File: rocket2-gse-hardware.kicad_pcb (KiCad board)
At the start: 4 copper layers, 118 x 135.2 mm, 194 parts, among them J1 USB_C Connector, Q1 n-MOSFET, Q10 n-MOSFET, Q2 n-MOSFET, Q3 n-MOSFET, Q4 n-MOSFET, Q5 n-MOSFET, Q6 n-MOSFET, Q7 n-MOSFET, Q8 n-MOSFET, Q9 n-MOSFET, Y1 16MHz

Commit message: finished pcb design of gse 1.0
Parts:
- removed PWR: Conn_01x02_Pin, TerminalBlock:TerminalBlock_bornier-2_P5.08mm
- removed S9: Solenoid, TerminalBlock:TerminalBlock_bornier-3_P5.08mm
- added C41: 100nF, Capacitor_SMD:C_0402_1005Metric, F.Cu at (200.5, 160.5)
- added C42: 100nF, Capacitor_SMD:C_0402_1005Metric, F.Cu at (185.5, 160.5)
- added D21: 3.3V, Diode_SMD:D_SOD-123, F.Cu at (99.0, 81.9)
- added D22: 1.0A, Diode_SMD:D_SMA, F.Cu at (91.5, 93.0)
- added D31: 3.3V, Diode_SMD:D_SOD-123, F.Cu at (99.1, 146.9)
- added D32: 5.1V, Diode_SMD:D_MiniMELF, F.Cu at (170.0, 143.5)
- added D33: 5.1V, Diode_SMD:D_MiniMELF, F.Cu at (131.0, 143.5)
- added D34: 5.1V, Diode_SMD:D_MiniMELF, F.Cu at (118.0, 143.5)
- added D35: 5.1V, Diode_SMD:D_MiniMELF, F.Cu at (144.0, 143.5)
- added D36: 5.1V, Diode_SMD:D_MiniMELF, F.Cu at (157.0, 143.5)
- added F1: Fuse Holder, Fuse:Fuseholder_Blade_Mini_Keystone_3568, F.Cu at (116.0, 28.3)
- added J2: ALARM, TerminalBlock:TerminalBlock_bornier-2_P5.08mm, F.Cu at (222.5, 162.0)
- added J3: USB_C Connector, Connector_USB:USB_C_Receptacle_GCT_USB4105-xx-A_16P_TopMnt_Horizontal, F.Cu at (171.0, 24.3)
- added J4: PWR, Connector_BarrelJack:BarrelJack_Horizontal, F.Cu at (142.0, 34.5)
- added J5: PWR, Connector_BarrelJack:BarrelJack_Horizontal, F.Cu at (157.0, 34.5)
- added J6: E-MATCH, TerminalBlock:TerminalBlock_bornier-2_P5.08mm, F.Cu at (197.0, 162.0)
- added J7: E-MATCH, TerminalBlock:TerminalBlock_bornier-2_P5.08mm, F.Cu at (182.0, 162.0)
- added PT4: Pressure Transducer 1, TerminalBlock:TerminalBlock_bornier-3_P5.08mm, F.Cu at (167.0, 163.1)
- added Q11: 30V 4A, Package_TO_SOT_SMD:SOT-23-3, F.Cu at (198.7, 153.1)
- added Q12: 30V 4A, Package_TO_SOT_SMD:SOT-23-3, F.Cu at (192.0, 153.2)
- added Q13: 30V 4A, Package_TO_SOT_SMD:SOT-23-3, F.Cu at (183.7, 153.1)
- added Q14: 30V 4A, Package_TO_SOT_SMD:SOT-23-3, F.Cu at (177.0, 153.2)
- added R54: 1K, Resistor_SMD:R_0402_1005Metric, F.Cu at (101.3, 143.8)
- added R55: 1K, Resistor_SMD:R_0402_1005Metric, F.Cu at (166.8, 148.0)
- added R56: 5K, Resistor_SMD:R_0402_1005Metric, F.Cu at (166.8, 140.0)
- added R57: 10K, Resistor_SMD:R_0402_1005Metric, F.Cu at (164.2, 140.0)
- added R58: 1K, Resistor_SMD:R_0402_1005Metric, F.Cu at (127.8, 148.0)
- added R59: 5K, Resistor_SMD:R_0402_1005Metric, F.Cu at (127.8, 140.0)
- added R60: 10K, Resistor_SMD:R_0402_1005Metric, F.Cu at (125.2, 140.0)
- added R61: 1K, Resistor_SMD:R_0402_1005Metric, F.Cu at (114.8, 148.0)
- added R62: 5K, Resistor_SMD:R_0402_1005Metric, F.Cu at (114.8, 140.0)
- added R63: 10K, Resistor_SMD:R_0402_1005Metric, F.Cu at (112.2, 140.0)
- added R64: 1K, Resistor_SMD:R_0402_1005Metric, F.Cu at (140.8, 148.0)
- added R65: 5K, Resistor_SMD:R_0402_1005Metric, F.Cu at (140.8, 140.0)
- added R66: 10K, Resistor_SMD:R_0402_1005Metric, F.Cu at (138.2, 140.0)
- added R67: 1K, Resistor_SMD:R_0402_1005Metric, F.Cu at (153.8, 148.0)
- added R68: 5K, Resistor_SMD:R_0402_1005Metric, F.Cu at (153.8, 140.0)
- added R69: 10K, Resistor_SMD:R_0402_1005Metric, F.Cu at (151.2, 140.0)
- added R70: 10K, Resistor_SMD:R_0402_1005Metric, F.Cu at (196.2, 153.9)
- added R71: 10K, Resistor_SMD:R_0402_1005Metric, F.Cu at (198.7, 150.0)
- added R72: 33K, Resistor_SMD:R_0402_1005Metric, F.Cu at (192.5, 156.1)
- added R73: 100, Resistor_SMD:R_0402_1005Metric, F.Cu at (192.5, 150.2)
- added R74: 10K, Resistor_SMD:R_0402_1005Metric, F.Cu at (190.0, 150.2)
- added R75: 10K, Resistor_SMD:R_0402_1005Metric, F.Cu at (181.2, 153.9)
- added R76: 10K, Resistor_SMD:R_0402_1005Metric, F.Cu at (183.7, 150.0)
- added R77: 33K, Resistor_SMD:R_0402_1005Metric, F.Cu at (177.5, 156.1)
- added R78: 100, Resistor_SMD:R_0402_1005Metric, F.Cu at (177.5, 150.2)
- added R79: 10K, Resistor_SMD:R_0402_1005Metric, F.Cu at (175.0, 150.2)
- added TP4: TestPoint, TestPoint:TestPoint_Pad_D2.0mm, F.Cu at (191.4, 88.8)
- added TP5: TestPoint, TestPoint:TestPoint_Pad_D2.0mm, F.Cu at (191.4, 93.8)
- added TP6: TestPoint, TestPoint:TestPoint_Pad_D2.0mm, F.Cu at (191.4, 98.8)
- C10: value 100nF -> 10uF
- C11, C13, C14, C9: value 100nF -> 1uF
- C25, C27: value 10nF -> 100nF
- C36: value 10uF -> 100nF
- C37: value 0.33uF -> 10nF
- C39, C8: value 1uF -> 10nF
- C40: value 1uF -> 100nF
- C6: value 4.7uF -> 100nF
- C7: value 10nF -> 4.7uF
- D1, D3, D5: value 1.0A -> LED; footprint Diode_SMD:D_SMA -> LED_SMD:LED_0603_1608Metric
- D10, D12, D6, D8: value 1.8V -> 3A 100V; footprint Diode_SMD:D_SOD-123 -> Diode_SMD:D_SMA
- D11, D13, D7, D9: value 1.0A -> 3A 100V
- D14, D16, D18, D20: value 1.8V -> 1.0A; footprint Diode_SMD:D_SOD-123 -> Diode_SMD:D_SMA
- D15, D17, D19: value 1.0A -> 3.3V; footprint Diode_SMD:D_SMA -> Diode_SMD:D_SOD-123
- D2, D4: value 1.8V -> LED; footprint Diode_SMD:D_SOD-123 -> LED_SMD:LED_0603_1608Metric
- D23, D25: value 5V -> 3.3V; footprint Diode_SMD:D_MiniMELF -> Diode_SMD:D_SOD-123
- D24, D26: value 5V -> 1.0A; footprint Diode_SMD:D_MiniMELF -> Diode_SMD:D_SMA
- D27, D29: value LED -> 3.3V; footprint LED_SMD:LED_0603_1608Metric -> Diode_SMD:D_SOD-123
- D28, D30: value LED -> 1.0A; footprint LED_SMD:LED_0603_1608Metric -> Diode_SMD:D_SMA
- J1: value USB_C Connector -> ARMING_PLUG; footprint Connector_USB:USB_C_Receptacle_GCT_USB4105-xx-A_16P_TopMnt_Horizontal -> TerminalBlock:TerminalBlock_bornier-2_P5.08mm
- Q1, Q10, Q2, Q3, Q4, Q5, Q6, Q7, Q8, Q9: value n-MOSFET -> 30V 4A
- R10: value 1K -> 3.3K
- R12, R24: value 1 -> 100; footprint Resistor_SMD:R_1206_3216Metric -> Resistor_SMD:R_0402_1005Metric
- R13, R7: value 1K -> 100K
- R14: value 10K -> 15K
- R15: value 1 -> 5K1; footprint Resistor_SMD:R_1206_3216Metric -> Resistor_SMD:R_0402_1005Metric
- R16: value 1K -> 5K1
- R17, R2: value 10K -> 100K
- R18, R9: value 1 -> 15K; footprint Resistor_SMD:R_1206_3216Metric -> Resistor_SMD:R_0402_1005Metric
- R19, R31, R35: value 1K -> 10K
- R20: value 10K -> 100
- R25, R41: value 1K -> 1; footprint Resistor_SMD:R_0402_1005Metric -> Resistor_SMD:R_1206_3216Metric
- R26, R5: value 10K -> 1K
- R27: value 1 -> 10K; footprint Resistor_SMD:R_1206_3216Metric -> Resistor_SMD:R_0402_1005Metric
- R28, R32: value 1K -> 100
- R29, R45: value 10K -> 1; footprint Resistor_SMD:R_0402_1005Metric -> Resistor_SMD:R_1206_3216Metric
- R3: value 1 -> 100K; footprint Resistor_SMD:R_1206_3216Metric -> Resistor_SMD:R_0402_1005Metric
- R30: value 1 -> 1K; footprint Resistor_SMD:R_1206_3216Metric -> Resistor_SMD:R_0402_1005Metric
- R33, R37: value 4.7K -> 1; footprint Resistor_SMD:R_0402_1005Metric -> Resistor_SMD:R_1206_3216Metric
- R34, R42: value 4.7K -> 1K
- R36, R40: value 4.7K -> 100
- R39, R43: value 4.7K -> 10K
- R4: value 1K -> 470
- R44: value 70K -> 100
- R46: value 100K -> 1K
- R47: value 100K -> 10K
- R48: value 470 -> 100
- R49: value 220 -> 1; footprint Resistor_SMD:R_0402_1005Metric -> Resistor_SMD:R_1206_3216Metric
- R50: value 470 -> 1K
- R51: value 2K -> 10K
- R52: value 5K1 -> 100
- R53: value 5K1 -> 1; footprint Resistor_SMD:R_0402_1005Metric -> Resistor_SMD:R_1206_3216Metric
- R6: value 1 -> 3.3K; footprint Resistor_SMD:R_1206_3216Metric -> Resistor_SMD:R_0402_1005Metric
- R8: value 10K -> 3.3K
- U16, U17, U18: footprint Package_SO:SOIC-8_3.9x4.9mm_P1.27mm -> Package_TO_SOT_SMD:SOT-23-6
- U2: footprint Package_TO_SOT_SMD:SOT-23-6 -> UCIRP-KiCAD-Lib:GC-XPORT
- U22: footprint UCIRP-KiCAD-Lib:GC-XPORT -> Package_SO:SOIC-8_3.9x4.9mm_P1.27mm
- U23: footprint Package_TO_SOT_SMD:SOT-89-3 -> Package_SO:SOIC-8_3.9x4.9mm_P1.27mm
- U24: footprint Package_TO_SOT_SMD:SOT-23-3 -> Package_SO:SOIC-8_3.9x4.9mm_P1.27mm
- U3: footprint Package_TO_SOT_SMD:SOT-23-6 -> Package_TO_SOT_SMD:SOT-89-3
- U4: footprint Package_TO_SOT_SMD:SOT-23-6 -> Package_TO_SOT_SMD:SOT-23-3
- moved Q1 165.1 mm to (221.7, 154.0)
- moved R7 148.1 mm to (210.0, 157.0), turned to 180 degrees
- moved R11 143.2 mm to (218.4, 155.1), turned to 0 degrees
- moved J1 141.0 mm to (210.5, 162.0)
- moved R12 136.9 mm to (218.4, 153.6), turned to 0 degrees
- moved R9 136.6 mm to (206.0, 157.0), turned to 180 degrees
- moved R53 125.1 mm to (95.1, 146.8), turned to -90 degrees
- moved R52 118.8 mm to (101.6, 141.5), turned to 180 degrees
- moved U16 114.4 mm to (114.2, 144.0), turned to 90 degrees
- moved C25 111.9 mm to (124.8, 143.4)
- moved C24 103.3 mm to (163.8, 143.4), turned to -90 degrees
- moved C26 102.3 mm to (111.8, 143.4), turned to -90 degrees
- moved C39 101.4 mm to (215.8, 141.9), turned to -90 degrees
- moved D30 99.3 mm to (91.6, 145.0), turned to 90 degrees
- moved C36 95.5 mm to (210.5, 98.5), turned to 180 degrees
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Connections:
- C11 pad 1: +3.3V -> +24V
- C12 pad 1: +3.3V -> +5V
- C13 pad 1: +3.3V -> +5V
- C20 pad 1: +5V -> +3.3V
- C21 pad 1: +5V -> +3.3V
- C22 pad 1: +5V -> +3.3V
- C23 pad 1: +5V -> +3.3V
- C24 pad 1: +3.3V -> +5V
- C25 pad 1: Net-(U16-T+) -> +5V
- C25 pad 2: Net-(U16-T-) -> GND
- C26 pad 1: +3.3V -> +5V
- C27 pad 1: Net-(U17-T+) -> +5V
- C27 pad 2: Net-(U17-T-) -> GND
- C28 pad 1: +3.3V -> +5V
- C29 pad 1: Net-(U18-T+) -> Net-(U19-T+)
- C29 pad 2: Net-(U18-T-) -> Net-(U19-T-)
- C31 pad 1: Net-(U19-T+) -> Net-(U20-T+)
- C31 pad 2: Net-(U19-T-) -> Net-(U20-T-)
- C33 pad 1: Net-(U20-T+) -> Net-(U21-T+)
- C33 pad 2: Net-(U20-T-) -> Net-(U21-T-)
- C35 pad 1: Net-(U21-T+) -> Net-(U22-T+)
- C35 pad 2: Net-(U21-T-) -> Net-(U22-T-)
- C37 pad 1: +24V -> Net-(U23-T+)
- C37 pad 2: GND -> Net-(U23-T-)
- C38 pad 1: +5V -> +3.3V
- C39 pad 1: +5V -> Net-(U24-T+)
- C39 pad 2: GND -> Net-(U24-T-)
- C4 pad 1: +3.3V -> nRST
- C9 pad 1: nRST -> +3.3V
- D1 pad 1: +24V -> GND
- D10 pad 1: Net-(D10-K) -> PWR0
- D10 pad 2: GND -> Net-(D10-A)
- D11 pad 1: +24V -> PWR0
- D11 pad 2: Net-(D11-A) -> Net-(D10-A)
- D12 pad 1: Net-(D12-K) -> PWR0
- D12 pad 2: GND -> Net-(D10-A)
- D13 pad 1: +24V -> PWR0
- D13 pad 2: Net-(D13-A) -> Net-(D10-A)
- D14 pad 1: Net-(D14-K) -> +24V
- D14 pad 2: GND -> Net-(D14-A)
- D15 pad 1: +24V -> Net-(D15-K)
- D15 pad 2: Net-(D15-A) -> GND
- D16 pad 1: Net-(D16-K) -> +24V
- D16 pad 2: GND -> Net-(D16-A)
- D17 pad 1: +24V -> Net-(D17-K)
- D17 pad 2: Net-(D17-A) -> GND
- D18 pad 1: Net-(D18-K) -> +24V
- D18 pad 2: GND -> Net-(D18-A)
- D19 pad 1: +24V -> Net-(D19-K)
- D19 pad 2: Net-(D19-A) -> GND
- D2 pad 1: Net-(D2-K) -> GND
- D2 pad 2: GND -> Net-(D2-A)
- D20 pad 1: Net-(D20-K) -> +24V
- D20 pad 2: GND -> Net-(D20-A)
- D24 pad 1: Net-(D24-K) -> +24V
- D24 pad 2: GND -> Net-(D24-A)
- D26 pad 1: Net-(D26-K) -> +24V
- D26 pad 2: GND -> Net-(D26-A)
- D27 pad 1: GND -> Net-(D27-K)
- D27 pad 2: Net-(D27-A) -> GND
- D28 pad 1: GND -> +24V
- D29 pad 1: GND -> Net-(D29-K)
- D29 pad 2: Net-(D29-A) -> GND
- D3 pad 1: +24V -> GND
- D30 pad 1: GND -> +24V
- D4 pad 1: Net-(D4-K) -> GND
- D4 pad 2: GND -> Net-(D4-A)
- D5 pad 1: +24V -> GND
- D6 pad 1: Net-(D6-K) -> PWR0
- D6 pad 2: GND -> Net-(D6-A)
- D7 pad 1: +24V -> PWR0
- D7 pad 2: Net-(D7-A) -> Net-(D6-A)
- D8 pad 1: Net-(D8-K) -> PWR0
- D8 pad 2: GND -> Net-(D6-A)
- D9 pad 1: +24V -> PWR0
- D9 pad 2: Net-(D9-A) -> Net-(D6-A)
- FB1 pad 1: Net-(TC0-+) -> Net-(TC1-+)
- FB1 pad 2: Net-(U16-T+) -> Net-(U19-T+)
- FB10 pad 2: Net-(U20-T-) -> Net-(U23-T-)
- FB11 pad 2: Net-(U21-T+) -> Net-(U24-T+)
- FB12 pad 2: Net-(U21-T-) -> Net-(U24-T-)
- FB2 pad 1: Net-(TC0--) -> Net-(TC1--)
- FB2 pad 2: Net-(U16-T-) -> Net-(U19-T-)
- FB3 pad 1: Net-(TC1-+) -> Net-(TC0-+)
- FB3 pad 2: Net-(U17-T+) -> Net-(U20-T+)
- FB4 pad 1: Net-(TC1--) -> Net-(TC0--)
- FB4 pad 2: Net-(U17-T-) -> Net-(U20-T-)
- FB5 pad 2: Net-(U18-T+) -> Net-(U21-T+)
- FB6 pad 2: Net-(U18-T-) -> Net-(U21-T-)
- FB7 pad 2: Net-(U19-T+) -> Net-(U22-T+)
- FB8 pad 2: Net-(U19-T-) -> Net-(U22-T-)
- FB9 pad 2: Net-(U20-T+) -> Net-(U23-T+)
- Q1 pad 1: S_EN0 -> Net-(Q1-G)
- Q1 pad 2: Net-(D1-A) -> GND
- Q1 pad 3: Net-(Q1-S) -> Net-(J2-Pin_2)
- Q10 pad 1: S_EN9 -> Net-(Q10-G)
- Q10 pad 2: Net-(D19-A) -> Net-(Q10-S)
- Q10 pad 3: Net-(Q10-S) -> Net-(D30-A)
- Q2 pad 1: S_EN1 -> Net-(Q2-G)
- Q2 pad 2: Net-(D3-A) -> Net-(Q2-S)
- Q2 pad 3: Net-(Q2-S) -> Net-(D14-A)
- Q3 pad 1: S_EN2 -> Net-(Q3-G)
- Q3 pad 2: Net-(D5-A) -> Net-(Q3-S)
- Q3 pad 3: Net-(Q3-S) -> Net-(D16-A)
- Q4 pad 1: S_EN3 -> Net-(Q4-G)
- Q4 pad 2: Net-(D7-A) -> Net-(Q4-S)
- Q4 pad 3: Net-(Q4-S) -> Net-(D18-A)
- Q5 pad 1: S_EN4 -> Net-(Q5-G)
- Q5 pad 2: Net-(D9-A) -> Net-(Q5-S)
- Q5 pad 3: Net-(Q5-S) -> Net-(D20-A)
- Q6 pad 1: S_EN5 -> Net-(Q6-G)
- Q6 pad 2: Net-(D11-A) -> Net-(Q6-S)
- Q6 pad 3: Net-(Q6-S) -> Net-(D22-A)
- Q7 pad 1: S_EN6 -> Net-(Q7-G)
- Q7 pad 2: Net-(D13-A) -> Net-(Q7-S)
- Q7 pad 3: Net-(Q7-S) -> Net-(D24-A)
- Q8 pad 1: S_EN7 -> Net-(Q8-G)
- Q8 pad 2: Net-(D15-A) -> Net-(Q8-S)
- Q8 pad 3: Net-(Q8-S) -> Net-(D26-A)
- Q9 pad 1: S_EN8 -> Net-(Q9-G)
- Q9 pad 2: Net-(D17-A) -> Net-(Q9-S)
- Q9 pad 3: Net-(Q9-S) -> Net-(D28-A)
- R10 pad 1: Net-(Q3-S) -> Net-(D3-A)
- R10 pad 2: Net-(D6-K) -> +24V
- R11 pad 1: S_EN3 -> ALARM_EN
- R12 pad 1: Net-(Q4-S) -> ALARM_EN
- R12 pad 2: GND -> Net-(Q1-G)
- R13 pad 1: Net-(Q4-S) -> Net-(D6-A)
- R13 pad 2: Net-(D8-K) -> PWR_READ0
- R14 pad 1: S_EN4 -> PWR_READ0
- R15 pad 1: Net-(Q5-S) -> GND
- R15 pad 2: GND -> Net-(J3-CC1)
- R16 pad 1: Net-(Q5-S) -> GND
- R16 pad 2: Net-(D10-K) -> Net-(J3-CC2)
- R17 pad 1: S_EN5 -> Net-(D10-A)
- R17 pad 2: GND -> PWR_READ1
- R18 pad 1: Net-(Q6-S) -> PWR_READ1
- R19 pad 1: Net-(Q6-S) -> S_EN0
- R19 pad 2: Net-(D12-K) -> GND
- R2 pad 1: S_EN0 -> +3.3V
- R2 pad 2: GND -> SWDIO
- R20 pad 1: S_EN6 -> S_EN0
- R20 pad 2: GND -> Net-(Q2-G)
- R21 pad 1: Net-(Q7-S) -> Net-(Q2-S)
- R22 pad 1: Net-(Q7-S) -> Net-(Q2-S)
- R22 pad 2: Net-(D14-K) -> Net-(D15-K)
- R23 pad 1: S_EN7 -> S_EN1
- R24 pad 1: Net-(Q8-S) -> S_EN1
- R24 pad 2: GND -> Net-(Q3-G)
- R25 pad 1: Net-(Q8-S) -> Net-(Q3-S)
- R25 pad 2: Net-(D16-K) -> GND
- R26 pad 1: S_EN8 -> Net-(Q3-S)
- R26 pad 2: GND -> Net-(D17-K)
- R27 pad 1: Net-(Q9-S) -> S_EN2
- R28 pad 1: Net-(Q9-S) -> S_EN2
- R28 pad 2: Net-(D18-K) -> Net-(Q4-G)
- R29 pad 1: S_EN9 -> Net-(Q4-S)
- R3 pad 1: Net-(Q1-S) -> GND
- R3 pad 2: GND -> SWCLK
- R30 pad 1: Net-(Q10-S) -> Net-(Q4-S)
- R30 pad 2: GND -> Net-(D19-K)
- R31 pad 1: Net-(Q10-S) -> S_EN3
- R31 pad 2: Net-(D20-K) -> GND
- R32 pad 1: Net-(PT0-Pin_2) -> S_EN3
- R32 pad 2: Net-(D24-K) -> Net-(Q5-G)
- R33 pad 1: Net-(U12--) -> Net-(Q5-S)
- R33 pad 2: PT0 -> GND
- R34 pad 1: PT0 -> Net-(Q5-S)
- R34 pad 2: GND -> Net-(D21-K)
- R35 pad 1: Net-(PT1-Pin_2) -> S_EN4
- R35 pad 2: Net-(D23-K) -> GND
- R36 pad 1: Net-(U13--) -> S_EN4
- R36 pad 2: PT1 -> Net-(Q6-G)
- R37 pad 1: PT1 -> Net-(Q6-S)
- R38 pad 1: Net-(PT2-Pin_2) -> Net-(Q6-S)
- R38 pad 2: Net-(D25-K) -> Net-(D23-K)
- R39 pad 1: Net-(U14--) -> S_EN5
- R39 pad 2: PT2 -> GND
- R4 pad 1: Net-(Q1-S) -> Net-(D1-A)
- R4 pad 2: Net-(D2-K) -> +3.3V
- R40 pad 1: PT2 -> S_EN5
- R40 pad 2: GND -> Net-(Q7-G)
- R41 pad 1: Net-(PT3-Pin_2) -> Net-(Q7-S)
- R41 pad 2: Net-(D26-K) -> GND
- R42 pad 1: Net-(U15--) -> Net-(Q7-S)
- R42 pad 2: PT3 -> Net-(D25-K)
- R43 pad 1: PT3 -> S_EN6
- R44 pad 1: +24V -> S_EN6
- R44 pad 2: PWR -> Net-(Q8-G)
- R45 pad 1: PWR -> Net-(Q8-S)
- R46 pad 1: +3.3V -> Net-(Q8-S)
- R46 pad 2: SWDIO -> Net-(D27-K)
- R47 pad 1: GND -> S_EN7
- R47 pad 2: SWCLK -> GND
- R48 pad 1: Net-(D27-A) -> S_EN7
- R48 pad 2: STATUS_LED -> Net-(Q9-G)
- R49 pad 1: Net-(D28-A) -> Net-(Q9-S)
- R49 pad 2: +3.3V -> GND
- R5 pad 1: S_EN1 -> Net-(D2-A)
- R5 pad 2: GND -> +5V
- R50 pad 1: Net-(D29-A) -> Net-(Q9-S)
- R50 pad 2: +5V -> Net-(D29-K)
- R51 pad 1: Net-(D30-A) -> S_EN8
- R51 pad 2: +24V -> GND
- R52 pad 1: GND -> S_EN8
- R52 pad 2: Net-(J1-CC1) -> Net-(Q10-G)
- R53 pad 1: GND -> Net-(Q10-S)
- R53 pad 2: Net-(J1-CC2) -> GND
- R6 pad 1: Net-(Q2-S) -> Net-(D4-A)
- R6 pad 2: GND -> PWR0
- R7 pad 1: Net-(Q2-S) -> ARM_POWER
- R7 pad 2: Net-(D4-K) -> ARM_CONT
- R8 pad 1: S_EN2 -> Net-(D5-A)
- R8 pad 2: GND -> PWR0
- R9 pad 1: Net-(Q3-S) -> ARM_CONT
- S0 pad 2: Net-(D1-A) -> Net-(D14-A)
- S1 pad 2: Net-(D3-A) -> Net-(D16-A)
- S2 pad 2: Net-(D5-A) -> Net-(D18-A)
- S3 pad 2: Net-(D7-A) -> Net-(D20-A)
- S4 pad 2: Net-(D9-A) -> Net-(D22-A)
- S5 pad 2: Net-(D11-A) -> Net-(D24-A)
- S6 pad 2: Net-(D13-A) -> Net-(D26-A)
- S7 pad 2: Net-(D15-A) -> Net-(D28-A)
- S8 pad 2: Net-(D17-A) -> Net-(D30-A)
- TP2 pad 1: +5V -> +3.3V
- TP3 pad 1: +3.3V -> +5V
- U1 pad 21: S_FB9 -> PT0
- U1 pad 22: PT0 -> PT1
- U1 pad 23: PT1 -> PT2
- U1 pad 24: PT2 -> PT3
- U1 pad 25: PT3 -> PT4
- U1 pad 26: PWR -> PWR_READ0
- U1 pad 27: STATUS_LED -> PWR_READ1
- U1 pad 33: ETH_CP2 -> ARM_CONT
- U1 pad 36: unconnected-(U1-PB15-Pad36) -> IGNITION1_OUTPUT
- U1 pad 37: unconnected-(U1-PC6-Pad37) -> IGNITION0_OUTPUT
- U1 pad 38: unconnected-(U1-PC7-Pad38) -> IGNITION1_CONT
- U1 pad 39: unconnected-(U1-PC8-Pad39) -> IGNITION0_CONT
- U1 pad 53: S_EN9 -> ALARM_EN
- U10 pad 1: S_FB8 -> S_FB5
- U10 pad 3: Net-(D18-K) -> Net-(D25-K)
- U10 pad 4: S_FB8 -> S_FB5
- U11 pad 1: S_FB9 -> S_FB6
- U11 pad 3: Net-(D20-K) -> Net-(D27-K)
- U11 pad 4: S_FB9 -> S_FB6
- U12 pad 1: Net-(U12--) -> S_FB7
- U12 pad 3: Net-(D24-K) -> Net-(D29-K)
- U12 pad 4: Net-(U12--) -> S_FB7
- U12 pad 5: +5V -> +3.3V
- U12 pad 6: +5V -> +3.3V
- U13 pad 1: Net-(U13--) -> S_FB8
- U13 pad 3: Net-(D23-K) -> Net-(D31-K)
- U13 pad 4: Net-(U13--) -> S_FB8
- U13 pad 5: +5V -> +3.3V
- U13 pad 6: +5V -> +3.3V
- U14 pad 3: Net-(D25-K) -> Net-(D32-K)
- U15 pad 3: Net-(D26-K) -> Net-(D33-K)
- U16 pad 1: GND -> Net-(U16--)
- U16 pad 2: Net-(U16-T-) -> GND
- U16 pad 3: Net-(U16-T+) -> Net-(D34-K)
- U16 pad 4: +3.3V -> Net-(U16--)
- U16 pad 5: TC_SPI1_SCK -> +5V
- U16 pad 6: nCS_0 -> +5V
- U17 pad 1: GND -> Net-(U17--)
- U17 pad 2: Net-(U17-T-) -> GND
- U17 pad 3: Net-(U17-T+) -> Net-(D35-K)
- U17 pad 4: +3.3V -> Net-(U17--)
- U17 pad 5: TC_SPI1_SCK -> +5V
- U17 pad 6: nCS_1 -> +5V
- U18 pad 1: GND -> Net-(U18--)
- U18 pad 2: Net-(U18-T-) -> GND
- U18 pad 3: Net-(U18-T+) -> Net-(D36-K)
- U18 pad 4: +3.3V -> Net-(U18--)
- U18 pad 5: TC_SPI1_SCK -> +5V
- U18 pad 6: nCS_2 -> +5V
- U19 pad 6: nCS_3 -> nCS_1
- U2 pad 1: S_FB0 -> GND
- U2 pad 2: GND -> +3.3V
- U2 pad 3: Net-(D2-K) -> ETH_nRST
- U2 pad 4: S_FB0 -> ETH_TX
- U2 pad 5: +3.3V -> ETH_RX
- U2 pad 6: +3.3V -> ETH_RTS
- U20 pad 6: nCS_4 -> nCS_0
- U21 pad 6: nCS_5 -> nCS_2
- U22 pad 2: +3.3V -> Net-(U22-T-)
- U22 pad 3: ETH_nRST -> Net-(U22-T+)
- U22 pad 4: ETH_TX -> +3.3V
- U22 pad 5: ETH_RX -> TC_SPI1_SCK
- U22 pad 6: ETH_RTS -> nCS_3
- U22 pad 7: ETH_CP2 -> TC_SPI1_SO
- U22 pad 8: ETH_CTS -> unconnected-(U22-Pad8)
- U23 pad 1: +5V -> GND
- U23 pad 2: GND -> Net-(U23-T-)
- U23 pad 3: +24V -> Net-(U23-T+)
- U24 pad 2: +3.3V -> Net-(U24-T-)
- U24 pad 3: +5V -> Net-(U24-T+)
- U3 pad 1: S_FB1 -> +5V
- U3 pad 3: Net-(D4-K) -> +24V
- U4 pad 1: S_FB2 -> GND
- U4 pad 2: GND -> +3.3V
- U4 pad 3: Net-(D6-K) -> +5V
- U5 pad 1: S_FB3 -> S_FB0
- U5 pad 3: Net-(D8-K) -> Net-(D15-K)
- U5 pad 4: S_FB3 -> S_FB0
- U6 pad 1: S_FB4 -> S_FB1
- U6 pad 3: Net-(D10-K) -> Net-(D17-K)
- U6 pad 4: S_FB4 -> S_FB1
- U7 pad 1: S_FB5 -> S_FB2
- U7 pad 3: Net-(D12-K) -> Net-(D19-K)
- U7 pad 4: S_FB5 -> S_FB2
- U8 pad 1: S_FB6 -> S_FB3
- U8 pad 3: Net-(D14-K) -> Net-(D21-K)
- U8 pad 4: S_FB6 -> S_FB3
- U9 pad 1: S_FB7 -> S_FB4
- U9 pad 3: Net-(D16-K) -> Net-(D23-K)
- U9 pad 4: S_FB7 -> S_FB4
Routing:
- net PWR0: track 0.00 -> 148.4 mm, vias 0 -> 2
- net +24V: track 631.0 -> 759.8 mm, vias 0 -> 1
- net ALARM_EN: track 0.00 -> 105.3 mm, vias 0 -> 2
- net IGNITION1_CONT: track 0.00 -> 96.9 mm, vias 0 -> 2
- net ARM_CONT: track 0.00 -> 91.0 mm, vias 0 -> 2
- net GND: track 108.7 -> 20.0 mm, vias 75 -> 102
- net IGNITION0_CONT: track 0.00 -> 84.2 mm, vias 0 -> 2
- net ETH_CP2: track 80.5 -> 0.00 mm, vias 4 -> 0
- net IGNITION1_OUTPUT: track 0.00 -> 78.4 mm, vias 0 -> 2
- net S_EN9: track 77.2 -> 0.00 mm, vias 2 -> 0
- net PWR: track 74.5 -> 0.00 mm, vias 2 -> 0
- net IGNITION0_OUTPUT: track 0.00 -> 73.9 mm, vias 0 -> 2
- net S_FB9: track 67.0 -> 0.00 mm
- net TC_SPI1_SO: track 154.5 -> 213.4 mm, vias 8 -> 2
- net PT4: track 0.00 -> 56.9 mm
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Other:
- board size 118 x 135.2 mm -> 173 x 147 mm
- board text added: "GSE 1.0 By Gavin Nguyen 3/1/2024"
- board text added: "PWR0"
- board text added: "PWR1"
- board text removed: "GSE 1.0 By Gavin Nguyen 2/21/2024"
- board text removed: "STATUS"

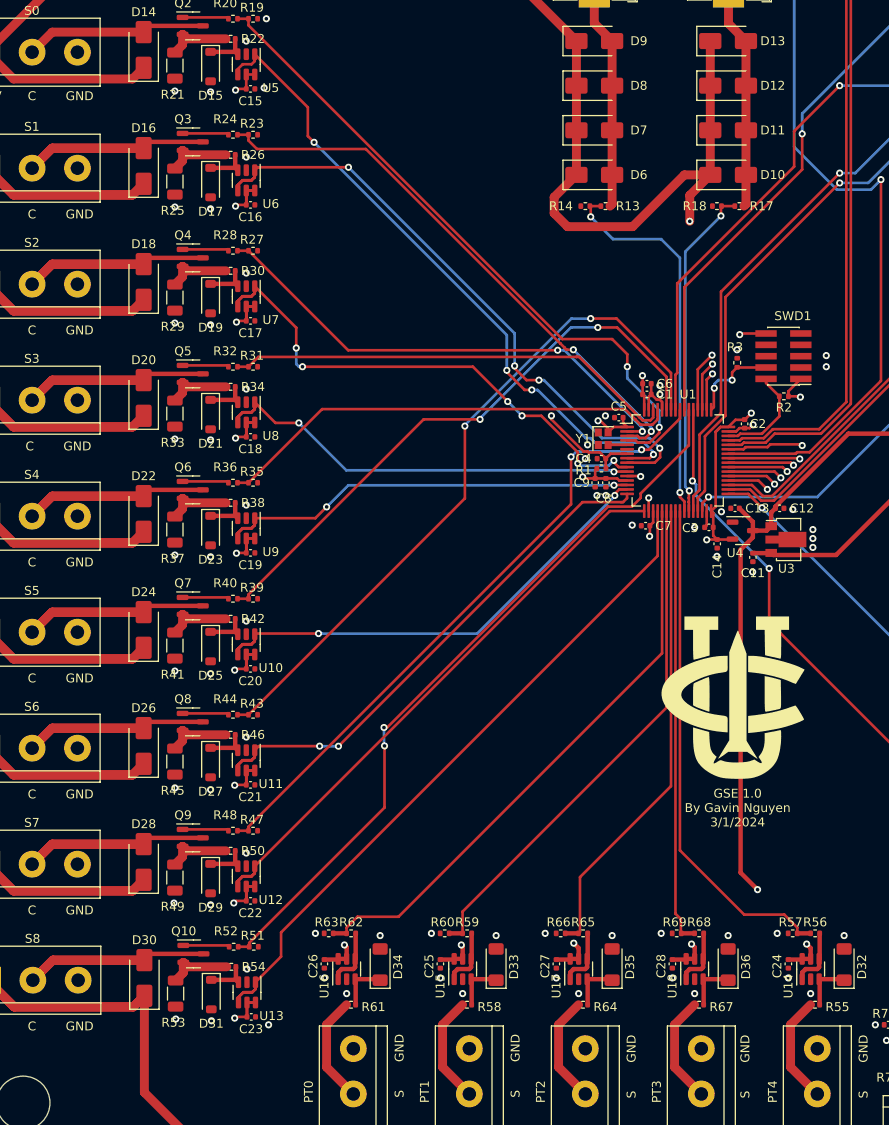
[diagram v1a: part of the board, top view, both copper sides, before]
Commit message: removed some thermal errors
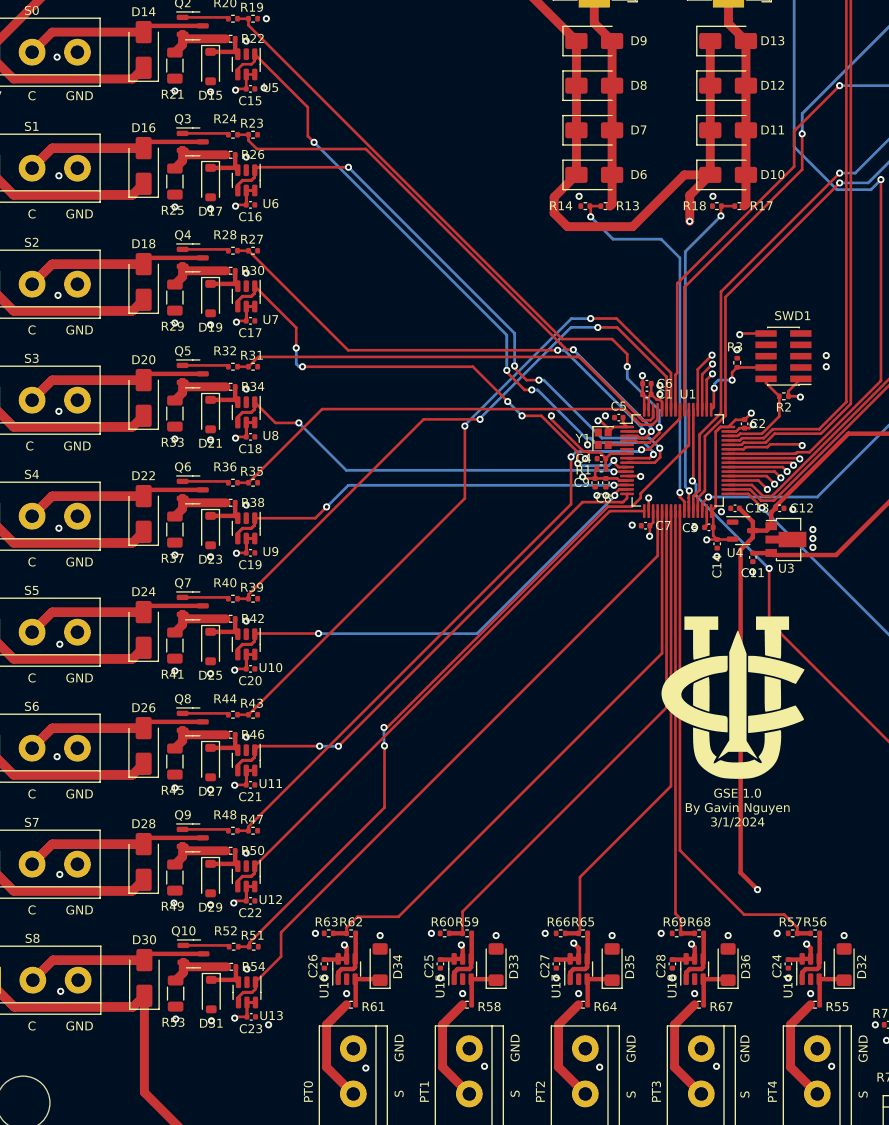
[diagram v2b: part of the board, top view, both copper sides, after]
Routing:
- net GND: vias 102 -> 118
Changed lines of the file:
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@@
   (segment (start 157.025299 83.75) (end 157.901041 83.75) (width 0.3) (layer "F.Cu") (net 2))
   (segment (start 145.675299 88.75) (end 147.15 88.75) (width 0.3) (layer "F.Cu") (net 2))
+  (via (at 81.8 41.8) (size 0.8) (drill 0.4) (layers "F.Cu" "B.Cu") (free) (net 2))
+  (via (at 81.8 120.2) (size 0.8) (drill 0.4) (layers "F.Cu" "B.Cu") (free) (net 2))
   (via (at 99 110.9) (size 0.8) (drill 0.4) (layers "F.Cu" "B.Cu") (free) (net 2))
   (via (at 99 84.7) (size 0.8) (drill 0.4) (layers "F.Cu" "B.Cu") (free) (net 2))
@@
   (via (at 178.25 40.75) (size 0.8) (drill 0.4) (layers "F.Cu" "B.Cu") (free) (net 2))
   (via (at 118 140.25) (size 0.8) (drill 0.4) (layers "F.Cu" "B.Cu") (free) (net 2))
+  (via (at 82.2 146.5) (size 0.8) (drill 0.4) (layers "F.Cu" "B.Cu") (free) (net 2))
   (via (at 210 57.25) (size 0.8) (drill 0.4) (layers "F.Cu" "B.Cu") (free) (net 2))
   (via (at 147.2 88.8) (size 0.8) (drill 0.4) (layers "F.Cu" "B.Cu") (net 2))
@@
   (via (at 95 110.6) (size 0.8) (drill 0.4) (layers "F.Cu" "B.Cu") (free) (net 2))
   (via (at 99 136.8) (size 0.8) (drill 0.4) (layers "F.Cu" "B.Cu") (free) (net 2))
+  (via (at 116.4 155.1) (size 0.8) (drill 0.4) (layers "F.Cu" "B.Cu") (free) (net 2))
   (via (at 136.5 140) (size 0.8) (drill 0.4) (layers "F.Cu" "B.Cu") (free) (net 2))
   (via (at 103 79) (size 0.8) (drill 0.4) (layers "F.Cu" "B.Cu") (free) (net 2))
@@
   (via (at 95 58.6) (size 0.8) (drill 0.4) (layers "F.Cu" "B.Cu") (free) (net 2))
   (via (at 153.25 94.5) (size 0.8) (drill 0.4) (layers "F.Cu" "B.Cu") (free) (net 2))
+  (via (at 155.3 57.4) (size 0.8) (drill 0.4) (layers "F.Cu" "B.Cu") (free) (net 2))
   (via (at 181 81.5) (size 0.8) (drill 0.4) (layers "F.Cu" "B.Cu") (free) (net 2))
   (via (at 144 140.25) (size 0.8) (drill 0.4) (layers "F.Cu" "B.Cu") (free) (net 2))
@@
   (via (at 205.5 155.75) (size 0.8) (drill 0.4) (layers "F.Cu" "B.Cu") (free) (net 2))
   (via (at 123.75 140) (size 0.8) (drill 0.4) (layers "F.Cu" "B.Cu") (free) (net 2))
+  (via (at 140.3 57.4) (size 0.8) (drill 0.4) (layers "F.Cu" "B.Cu") (free) (net 2))
   (via (at 103 53) (size 0.8) (drill 0.4) (layers "F.Cu" "B.Cu") (free) (net 2))
   (via (at 95 123.7) (size 0.8) (drill 0.4) (layers "F.Cu" "B.Cu") (free) (net 2))
@@
   (via (at 163.75 145) (size 0.8) (drill 0.4) (layers "F.Cu" "B.Cu") (free) (net 2))
   (via (at 174.75 152) (size 0.8) (drill 0.4) (layers "F.Cu" "B.Cu") (free) (net 2))
+  (via (at 168.6 154.9) (size 0.8) (drill 0.4) (layers "F.Cu" "B.Cu") (free) (net 2))
   (via (at 149.5 140) (size 0.8) (drill 0.4) (layers "F.Cu" "B.Cu") (free) (net 2))
   (via (at 168 76.5) (size 0.8) (drill 0.4) (layers "F.Cu" "B.Cu") (free) (net 2))
   (via (at 103.08 144) (size 0.8) (drill 0.4) (layers "F.Cu" "B.Cu") (free) (net 2))
+  (via (at 82 94.6) (size 0.8) (drill 0.4) (layers "F.Cu" "B.Cu") (free) (net 2))
   (via (at 220.75 156.25) (size 0.8) (drill 0.4) (layers "F.Cu" "B.Cu") (free) (net 2))
   (via (at 148.1 91.2) (size 0.8) (drill 0.4) (layers "F.Cu" "B.Cu") (net 2))
@@
   (via (at 110.75 140) (size 0.8) (drill 0.4) (layers "F.Cu" "B.Cu") (free) (net 2))
   (via (at 159.75 99.5) (size 0.8) (drill 0.4) (layers "F.Cu" "B.Cu") (free) (net 2))
+  (via (at 82 55.1) (size 0.8) (drill 0.4) (layers "F.Cu" "B.Cu") (free) (net 2))
+  (via (at 81.9 68.5) (size 0.8) (drill 0.4) (layers "F.Cu" "B.Cu") (free) (net 2))
   (via (at 166.5 95.75) (size 0.8) (drill 0.4) (layers "F.Cu" "B.Cu") (free) (net 2))
   (via (at 166.25 146.75) (size 0.8) (drill 0.4) (layers "F.Cu" "B.Cu") (free) (net 2))
   (via (at 213 143.75) (size 0.8) (drill 0.4) (layers "F.Cu" "B.Cu") (free) (net 2))
   (via (at 178.5 42.75) (size 0.8) (drill 0.4) (layers "F.Cu" "B.Cu") (free) (net 2))
+  (via (at 82.1 133.4) (size 0.8) (drill 0.4) (layers "F.Cu" "B.Cu") (free) (net 2))
   (via (at 141.25 85.25) (size 0.8) (drill 0.4) (layers "F.Cu" "B.Cu") (free) (net 2))
   (via (at 99 45.7) (size 0.8) (drill 0.4) (layers "F.Cu" "B.Cu") (free) (net 2))
@@
   (via (at 99.1 149.8) (size 0.8) (drill 0.4) (layers "F.Cu" "B.Cu") (free) (net 2))
   (via (at 181 77.5) (size 0.8) (drill 0.4) (layers "F.Cu" "B.Cu") (free) (net 2))
+  (via (at 82.1 107.6) (size 0.8) (drill 0.4) (layers "F.Cu" "B.Cu") (free) (net 2))
   (via (at 95 45.6) (size 0.8) (drill 0.4) (layers "F.Cu" "B.Cu") (free) (net 2))
   (via (at 198.25 42.75) (size 0.8) (drill 0.4) (layers "F.Cu" "B.Cu") (free) (net 2))
+  (via (at 82 81.5) (size 0.8) (drill 0.4) (layers "F.Cu" "B.Cu") (free) (net 2))
   (via (at 189.25 74) (size 0.8) (drill 0.4) (layers "F.Cu" "B.Cu") (free) (net 2))
   (via (at 105 45.25) (size 0.8) (drill 0.4) (layers "F.Cu" "B.Cu") (free) (net 2))
@@
   (via (at 103 66) (size 0.8) (drill 0.4) (layers "F.Cu" "B.Cu") (free) (net 2))
   (via (at 210 37.25) (size 0.8) (drill 0.4) (layers "F.Cu" "B.Cu") (free) (net 2))
+  (via (at 142.6 155) (size 0.8) (drill 0.4) (layers "F.Cu" "B.Cu") (free) (net 2))
   (via (at 170 140.25) (size 0.8) (drill 0.4) (layers "F.Cu" "B.Cu") (free) (net 2))
+  (via (at 155.7 154.9) (size 0.8) (drill 0.4) (layers "F.Cu" "B.Cu") (free) (net 2))
   (via (at 213 43.75) (size 0.8) (drill 0.4) (layers "F.Cu" "B.Cu") (free) (net 2))
   (via (at 95 71.6) (size 0.8) (drill 0.4) (layers "F.Cu" "B.Cu") (free) (net 2))
+  (via (at 129.7 154.9) (size 0.8) (drill 0.4) (layers "F.Cu" "B.Cu") (free) (net 2))
   (via (at 210.25 137.25) (size 0.8) (drill 0.4) (layers "F.Cu" "B.Cu") (free) (net 2))
   (via (at 140.25 146.75) (size 0.8) (drill 0.4) (layers "F.Cu" "B.Cu") (free) (net 2))
@@
   (via (at 155.2 75.2) (size 0.8) (drill 0.4) (layers "F.Cu" "B.Cu") (net 127))
   (via (at 203.6 41.6) (size 0.8) (drill 0.4) (layers "F.Cu" "B.Cu") (net 127))
+  (segment (start 155.2 75.2) (end 155.35 75.35) (width 0.3) (layer "In1.Cu") (net 127))
+  (segment (start 200.7 41.6) (end 203.6 41.6) (width 0.3) (layer "In1.Cu") (net 127))
   (segment (start 155.35 75.35) (end 166.132233 75.35) (width 0.3) (layer "In1.Cu") (net 127))
-  (segment (start 201.7 43.5) (end 203.6 41.6) (width 0.3) (layer "In1.Cu") (net 127))
+  (segment (start 180.582233 60.9) (end 181.4 60.9) (width 0.3) (layer "In1.Cu") (net 127))
   (segment (start 166.132233 75.35) (end 180.582233 60.9) (width 0.3) (layer "In1.Cu") (net 127))
-  (segment (start 180.582233 60.9) (end 181.4 60.9) (width 0.3) (layer "In1.Cu") (net 127))
-  (segment (start 198.8 43.5) (end 201.7 43.5) (width 0.3) (layer "In1.Cu") (net 127))
-  (segment (start 155.2 75.2) (end 155.35 75.35) (width 0.3) (layer "In1.Cu") (net 127))
-  (segment (start 181.4 60.9) (end 198.8 43.5) (width 0.3) (layer "In1.Cu") (net 127))
+  (segment (start 181.4 60.9) (end 200.7 41.6) (width 0.3) (layer "In1.Cu") (net 127))
   (segment (start 209.3 76.845) (end 206.05 80.095) (width 0.3) (layer "F.Cu") (net 128))
   (segment (start 208.5 82.132893) (end 208.5 97.595) (width 0.3) (layer "F.Cu") (net 128))

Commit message: fixed planes
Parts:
- moved C12 88.9 mm to (98.5, 153.8)
- moved U3 88.3 mm to (100.0, 157.0)
- moved C11 87.5 mm to (96.2, 158.0), turned to 90 degrees
- moved C13 48.0 mm to (146.5, 139.0), turned to 0 degrees
- moved U4 43.0 mm to (146.0, 136.0), turned to -90 degrees
- moved C14 37.9 mm to (146.0, 133.0), turned to 0 degrees
- moved D6 17.8 mm to (131.0, 41.0), turned to 90 degrees
- moved D10 15.1 mm to (151.2, 41.0), turned to 90 degrees
- moved R18 10.9 mm to (153.0, 48.0)
- moved R17 10.9 mm to (155.5, 48.0)
- moved D7 10.8 mm to (136.0, 41.0), turned to 90 degrees
- moved R13 10.6 mm to (141.9, 48.0)
- moved R14 10.6 mm to (139.7, 48.0)
- moved D11 9.06 mm to (156.0, 41.0), turned to 90 degrees
- moved D13 8.56 mm to (165.5, 41.0), turned to 90 degrees
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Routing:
- net +24V: track 759.8 -> 114.6 mm, vias 1 -> 3
- net PWR0: track 148.4 -> 105.4 mm, vias 2 -> 6
- net GND: track 20.0 -> 49.8 mm, vias 118 -> 115
- net Net-(D6-A): track 24.9 -> 10.7 mm
- net Net-(D16-A): track 33.8 -> 20.4 mm
- net Net-(D10-A): track 24.9 -> 12.3 mm
- net PWR_READ1: track 37.6 -> 49.5 mm
- net PWR_READ0: track 43.0 -> 54.2 mm
- net +3.3V: track 159.1 -> 158.2 mm
- net +5V: track 109.0 -> 109.6 mm, vias 6 -> 9
- added copper zone on F.Cu, net +24V
- added copper zone on In2.Cu, net +24V
- added copper zone on F.Cu, net Net-(D10-A)
- added copper zone on F.Cu, net Net-(D6-A)
- added copper zone on F.Cu, net PWR0
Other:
- outline, holes or cut-outs redrawn
